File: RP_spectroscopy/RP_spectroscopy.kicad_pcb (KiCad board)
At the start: 2 copper layers, 90.5 x 111 mm, 79 parts, among them J1 Extension connector 1, J10 Conn_Coaxial, J2 Extension connector 2, J3 Conn_Coaxial, J4 Conn_Coaxial, J5 Conn_Coaxial, J6 Conn_Coaxial, J7 Molex PicoBlade, J8 Molex PicoBlade, J9 Conn_Coaxial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

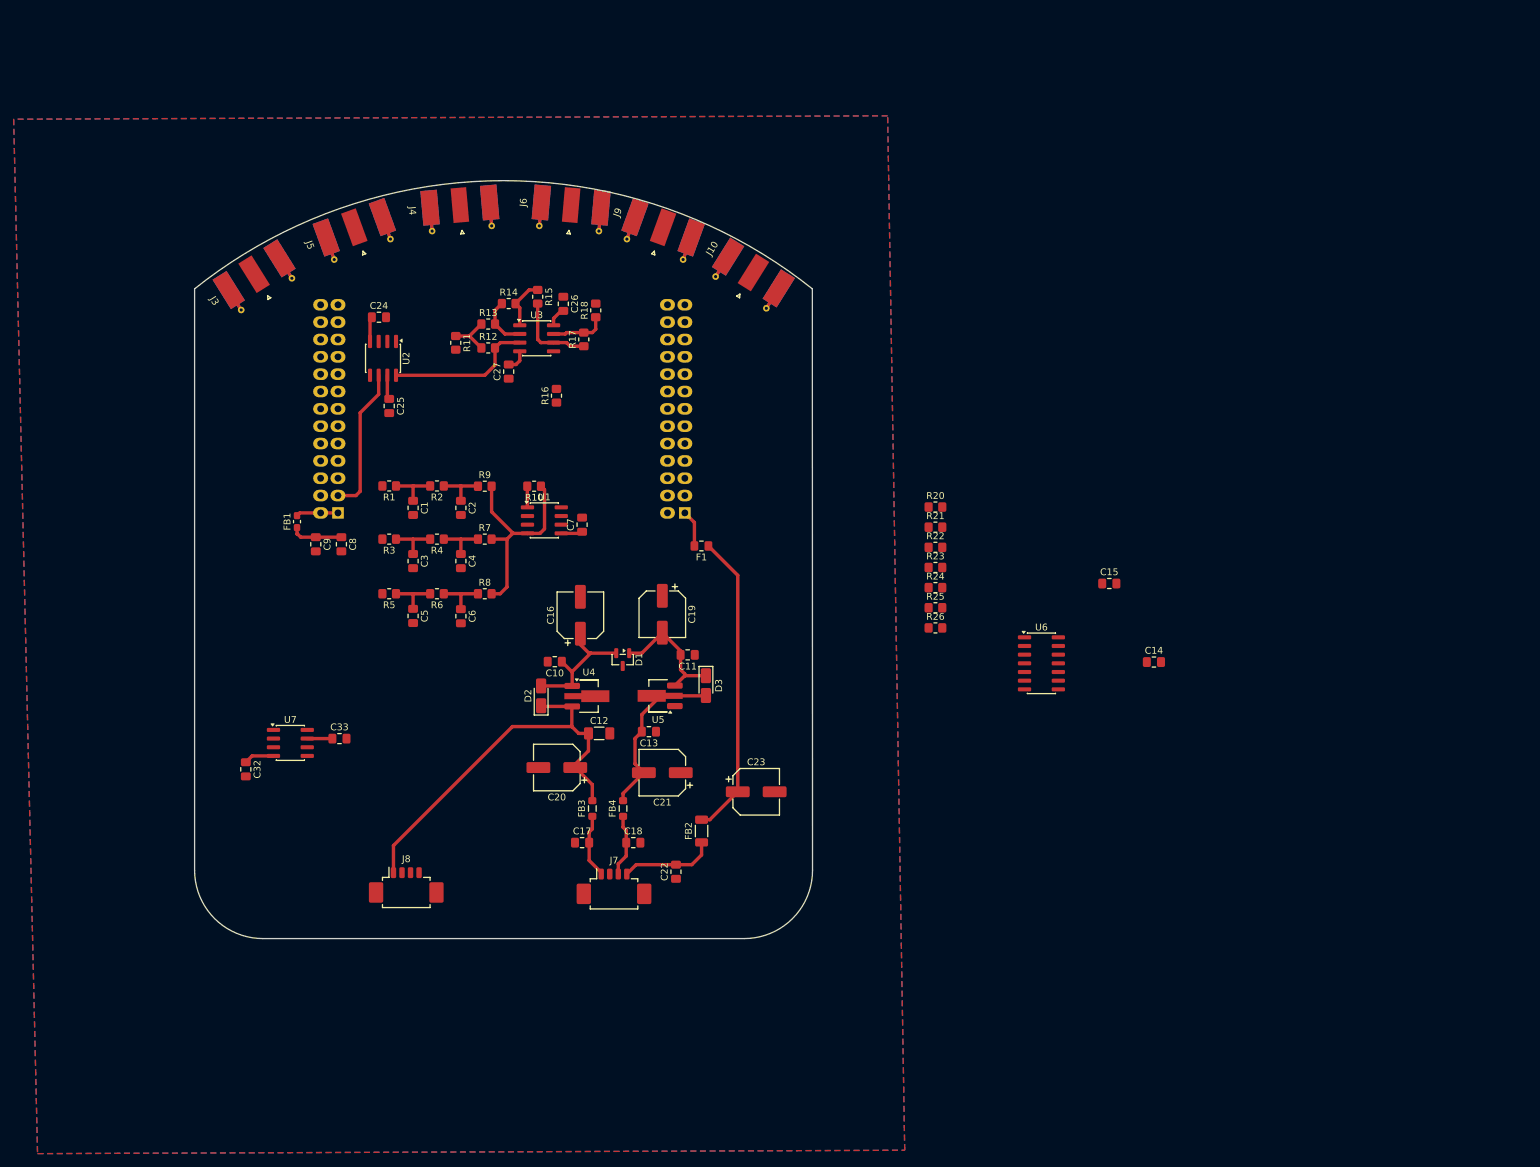
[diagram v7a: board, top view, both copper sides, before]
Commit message: Finished the wirings of everything apart from the BP filter and amplification
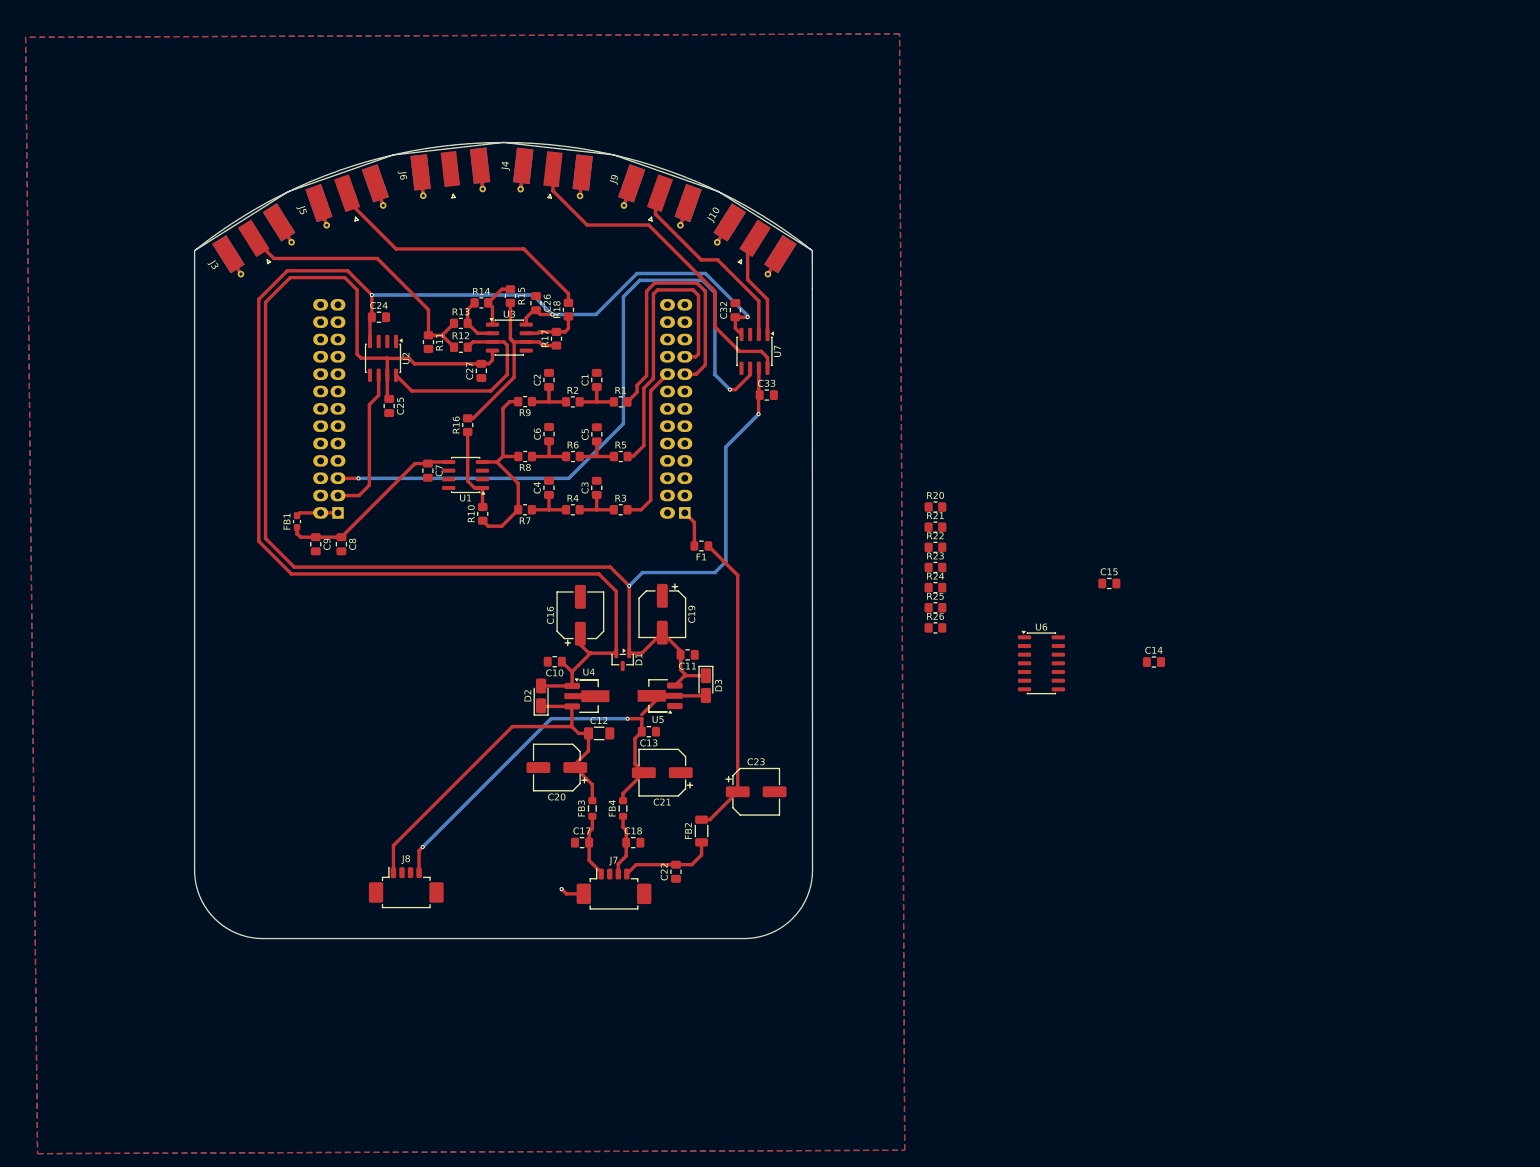
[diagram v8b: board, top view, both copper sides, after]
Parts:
- moved C32 98.3 mm to (169.2, 58.0), turned to 90 degrees
- moved U7 88.9 mm to (172.0, 64.0), turned to -90 degrees
- moved C33 80.3 mm to (173.8, 70.4)
- moved R5 39.4 mm to (152.4, 79.4), turned to 0 degrees
- moved C5 37.8 mm to (148.9, 76.2), turned to 90 degrees
- moved R1 36.1 mm to (152.4, 71.4), turned to 0 degrees
- moved R3 34.2 mm to (152.4, 87.2), turned to 0 degrees
- moved C1 32.8 mm to (148.9, 68.2), turned to 90 degrees
- moved C6 29.6 mm to (141.9, 76.1), turned to 90 degrees
- moved C3 29.0 mm to (148.9, 84.0), turned to 90 degrees
- moved R6 28.3 mm to (145.4, 79.4), turned to 0 degrees
- moved C7 23.9 mm to (124.2, 81.5), turned to -90 degrees
- moved R2 23.4 mm to (145.4, 71.4), turned to 0 degrees
- moved C2 22.7 mm to (141.9, 68.2), turned to 90 degrees
- moved R8 21.0 mm to (138.4, 79.4), turned to 180 degrees
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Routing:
- net -5VA: track 29.4 -> 218.6 mm, vias 0 -> 2
- net +5VA: track 31.0 -> 218.2 mm, vias 0 -> 3
- net Multiplex switch: track 0.00 -> 98.8 mm, vias 0 -> 2
- net Differential PD: track 0.00 -> 49.3 mm
- net Small offset: track 0.00 -> 43.8 mm
- net -15V: track 25.4 -> 68.6 mm, vias 0 -> 2
- net Slow integrator: track 0.00 -> 41.3 mm
- net Summed signals: track 0.00 -> 40.4 mm
- net Sweep/Fast PID: track 6.95 -> 40.6 mm
- net +/- PD: track 0.00 -> 28.6 mm
- net Big offset: track 0.00 -> 23.5 mm
- net +3V3: track 10.8 -> 27.9 mm
- net DC PD demultiplexed signal: track 0.00 -> 15.8 mm
- net Net-(U3B--): track 12.4 -> 27.6 mm
- net Net-(R10-Pad2): track 3.11 -> 12.6 mm
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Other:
- board size 90.5 x 111 mm -> 90.5 x 116.6 mm
